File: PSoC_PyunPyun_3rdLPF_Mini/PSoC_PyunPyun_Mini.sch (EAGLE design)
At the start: 28 parts, among them IC1 LM358N

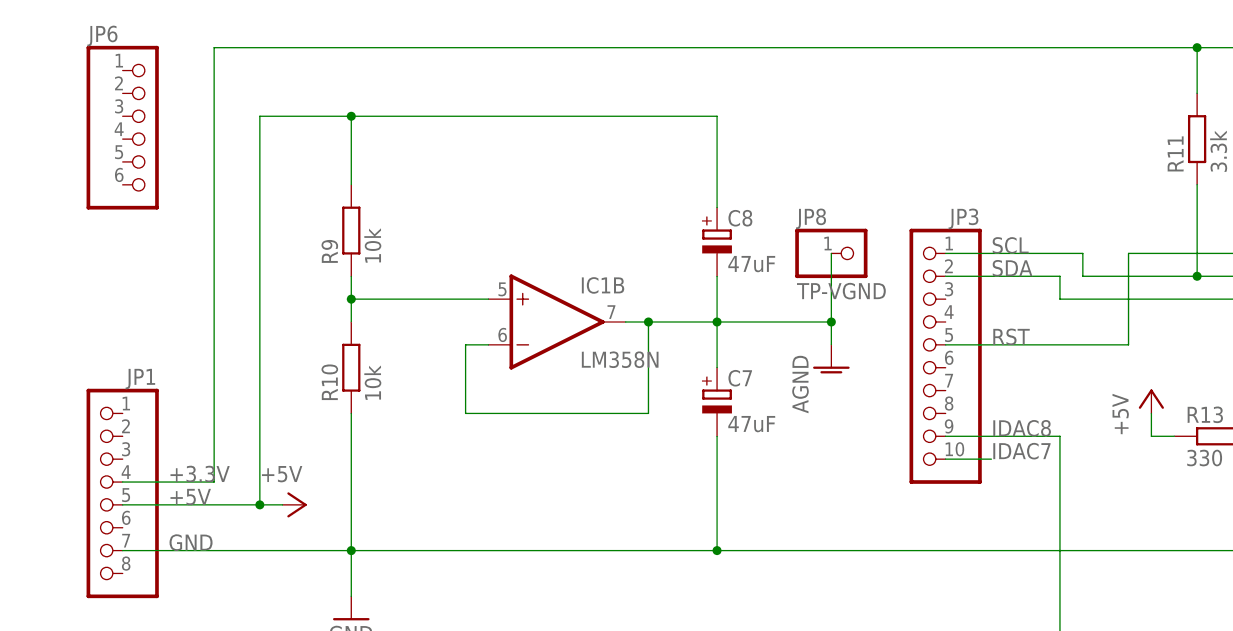
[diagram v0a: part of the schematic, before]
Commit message: PSoC_Pyun_Pyun_Mini 回路図、基板図修正
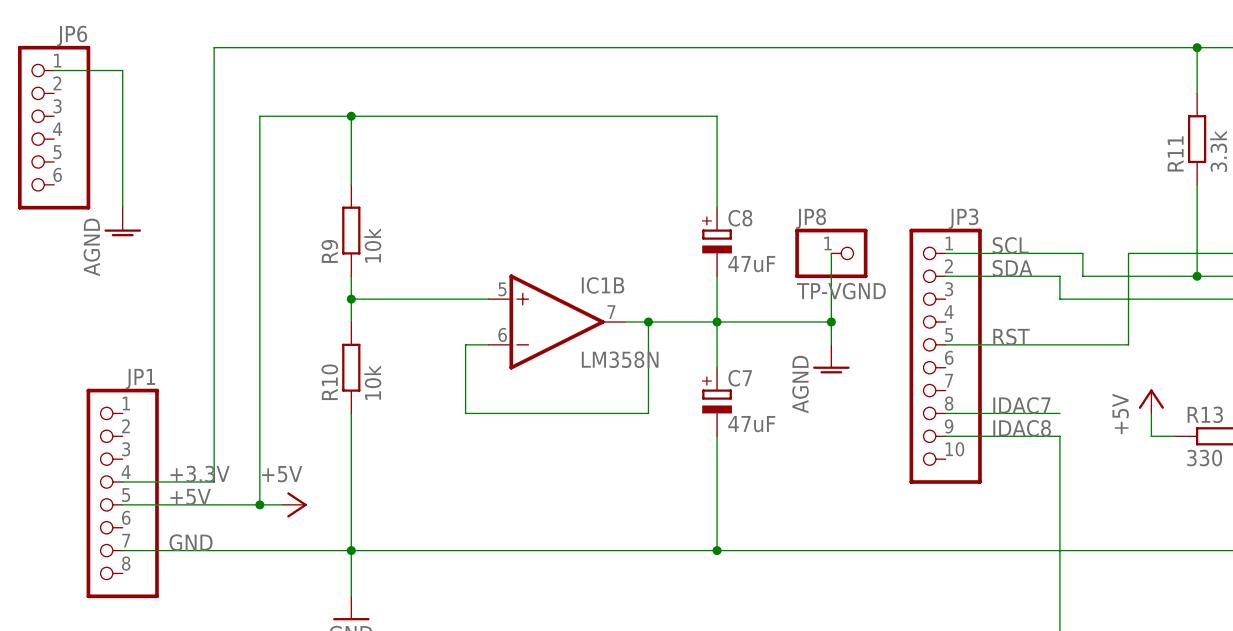
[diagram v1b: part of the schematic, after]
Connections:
- net AGND: now also JP6.1
- net IDAC7: now also JP3.8; no longer JP3.10
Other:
- moved on the sheet: JP6
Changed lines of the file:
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@@
 <part name="JP8" library="pinhead" deviceset="PINHD-1X1" device="" value="TP-VGND"/>
 <part name="JP9" library="pinhead" deviceset="PINHD-1X1" device="" value="TP-GND"/>
+<part name="AGND3" library="supply1" deviceset="AGND" device=""/>
 </parts>
 <sheets>
@@
 <instance part="P+3" gate="1" x="157.48" y="76.2"/>
 <instance part="GND2" gate="VR1" x="170.18" y="45.72"/>
-<instance part="JP6" gate="A" x="12.7" y="144.78"/>
+<instance part="JP6" gate="A" x="0" y="144.78" rot="MR0"/>
 <instance part="IC1" gate="A" x="93.98" y="66.04"/>
 <instance part="IC1" gate="B" x="58.42" y="124.46"/>
@@
 <instance part="JP8" gate="G$1" x="91.44" y="132.08"/>
 <instance part="JP9" gate="G$1" x="154.94" y="96.52"/>
+<instance part="AGND3" gate="VR1" x="10.16" y="134.62"/>
 </instances>
 <busses>
@@
 <wire x1="170.18" y1="55.88" x2="170.18" y2="48.26" width="0.1524" layer="91"/>
 </segment>
+<segment>
+<pinref part="JP6" gate="A" pin="1"/>
+<pinref part="AGND3" gate="VR1" pin="AGND"/>
+<wire x1="2.54" y1="152.4" x2="10.16" y2="152.4" width="0.1524" layer="91"/>
+<wire x1="10.16" y1="152.4" x2="10.16" y2="137.16" width="0.1524" layer="91"/>
+</segment>
 </net>
 <net name="+3.3V" class="0">
@@
 <net name="IDAC7" class="0">
 <segment>
-<pinref part="JP3" gate="A" pin="10"/>
-<wire x1="101.6" y1="109.22" x2="106.68" y2="109.22" width="0.1524" layer="91"/>
-<label x="106.68" y="109.22" size="1.778" layer="95"/>
-</segment>
-</net>
+<pinref part="JP3" gate="A" pin="8"/>
+<wire x1="101.6" y1="114.3" x2="114.3" y2="114.3" width="0.1524" layer="91"/>
+<label x="106.68" y="114.3" size="1.778" layer="95"/>
+</segment>
+</net>

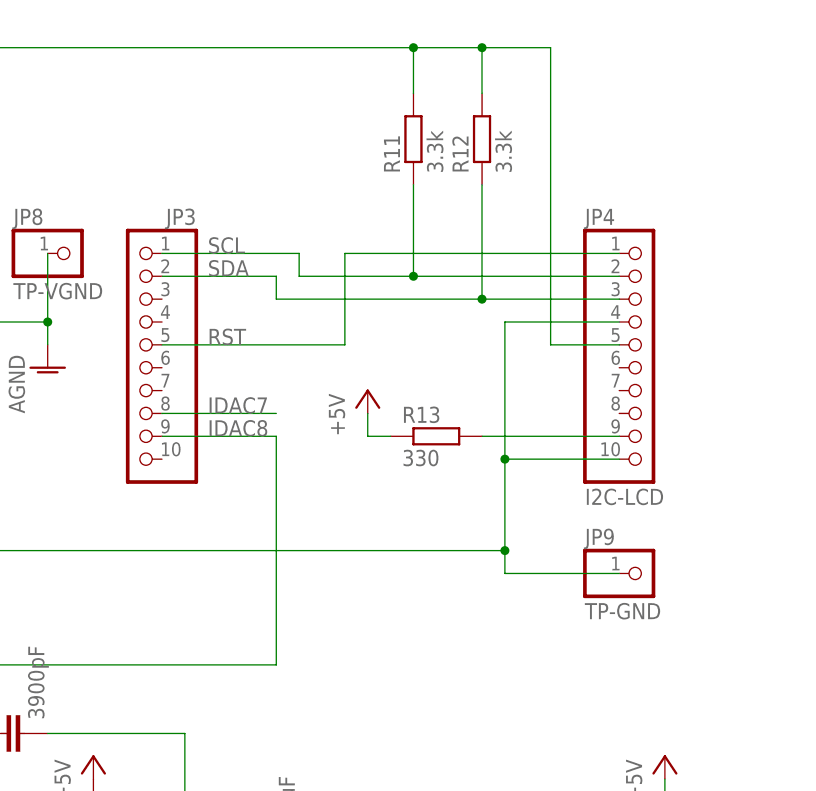
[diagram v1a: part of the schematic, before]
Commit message: PSoC_Pyun_Pyun_3rdLPF_Mini: Change LCD to aitendo
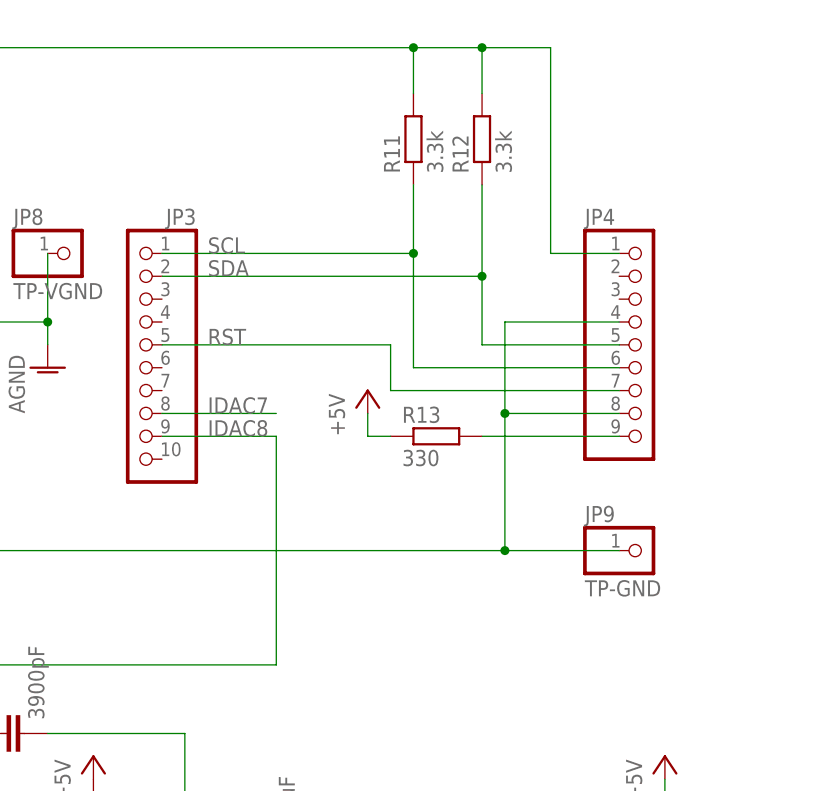
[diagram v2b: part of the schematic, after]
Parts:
- JP4: value I2C-LCD -> (none); device pinhead:PINHD-1X10 -> pinhead:PINHD-1X9
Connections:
- net +3.3V: now also JP4.1; no longer JP4.5
- net GND: now also JP4.8; no longer JP4.10
- net RST: now also JP4.7; no longer JP4.1
- net SCL: now also JP4.6; no longer JP4.2
- net SDA: now also JP4.5; no longer JP4.3
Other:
- moved on the sheet: JP9
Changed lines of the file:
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@@
 <part name="JP2" library="pinhead" deviceset="PINHD-1X8" device=""/>
 <part name="JP3" library="pinhead" deviceset="PINHD-1X10" device=""/>
-<part name="JP4" library="pinhead" deviceset="PINHD-1X10" device="" value="I2C-LCD"/>
 <part name="R1" library="rcl" deviceset="R-EU_" device="0207/7" value="100k"/>
 <part name="R2" library="rcl" deviceset="R-EU_" device="0207/7" value="33k"/>
@@
 <part name="JP9" library="pinhead" deviceset="PINHD-1X1" device="" value="TP-GND"/>
 <part name="AGND3" library="supply1" deviceset="AGND" device=""/>
+<part name="JP4" library="pinhead" deviceset="PINHD-1X9" device=""/>
 </parts>
 <sheets>
@@
 <instance part="JP2" gate="A" x="7.62" y="58.42" rot="MR0"/>
 <instance part="JP3" gate="A" x="99.06" y="121.92" rot="MR0"/>
-<instance part="JP4" gate="A" x="154.94" y="121.92"/>
 <instance part="R1" gate="G$1" x="55.88" y="68.58"/>
 <instance part="R2" gate="G$1" x="71.12" y="68.58"/>
@@
 <instance part="C4" gate="G$1" x="48.26" y="60.96"/>
 <instance part="JP8" gate="G$1" x="91.44" y="132.08"/>
-<instance part="JP9" gate="G$1" x="154.94" y="96.52"/>
+<instance part="JP9" gate="G$1" x="154.94" y="99.06"/>
 <instance part="AGND3" gate="VR1" x="10.16" y="134.62"/>
+<instance part="JP4" gate="A" x="154.94" y="121.92"/>
 </instances>
 <busses>
@@
 <wire x1="76.2" y1="99.06" x2="139.7" y2="99.06" width="0.1524" layer="91"/>
 <junction x="76.2" y="99.06"/>
-<wire x1="139.7" y1="99.06" x2="139.7" y2="109.22" width="0.1524" layer="91"/>
-<pinref part="JP4" gate="A" pin="4"/>
-<wire x1="139.7" y1="109.22" x2="139.7" y2="124.46" width="0.1524" layer="91"/>
+<wire x1="139.7" y1="99.06" x2="139.7" y2="114.3" width="0.1524" layer="91"/>
+<wire x1="139.7" y1="114.3" x2="139.7" y2="124.46" width="0.1524" layer="91"/>
 <wire x1="139.7" y1="124.46" x2="152.4" y2="124.46" width="0.1524" layer="91"/>
 <pinref part="GND1" gate="1" pin="GND"/>
 <wire x1="35.56" y1="93.98" x2="35.56" y2="99.06" width="0.1524" layer="91"/>
-<pinref part="JP4" gate="A" pin="10"/>
-<wire x1="152.4" y1="109.22" x2="139.7" y2="109.22" width="0.1524" layer="91"/>
-<junction x="139.7" y="109.22"/>
 <pinref part="JP9" gate="G$1" pin="1"/>
-<wire x1="152.4" y1="96.52" x2="139.7" y2="96.52" width="0.1524" layer="91"/>
-<wire x1="139.7" y1="96.52" x2="139.7" y2="99.06" width="0.1524" layer="91"/>
+<wire x1="152.4" y1="99.06" x2="139.7" y2="99.06" width="0.1524" layer="91"/>
 <junction x="139.7" y="99.06"/>
+<pinref part="JP4" gate="A" pin="4"/>
+<pinref part="JP4" gate="A" pin="8"/>
+<wire x1="152.4" y1="114.3" x2="139.7" y2="114.3" width="0.1524" layer="91"/>
+<junction x="139.7" y="114.3"/>
 </segment>
 <segment>
@@
 <wire x1="129.54" y1="154.94" x2="137.16" y2="154.94" width="0.1524" layer="91"/>
 <wire x1="137.16" y1="154.94" x2="144.78" y2="154.94" width="0.1524" layer="91"/>
-<wire x1="144.78" y1="154.94" x2="144.78" y2="121.92" width="0.1524" layer="91"/>
-<pinref part="JP4" gate="A" pin="5"/>
-<wire x1="144.78" y1="121.92" x2="152.4" y2="121.92" width="0.1524" layer="91"/>
 <pinref part="R11" gate="G$1" pin="2"/>
 <wire x1="129.54" y1="149.86" x2="129.54" y2="154.94" width="0.1524" layer="91"/>
@@
 <junction x="137.16" y="154.94"/>
 <label x="15.24" y="106.68" size="1.778" layer="95"/>
+<wire x1="144.78" y1="154.94" x2="144.78" y2="132.08" width="0.1524" layer="91"/>
+<pinref part="JP4" gate="A" pin="1"/>
+<wire x1="144.78" y1="132.08" x2="152.4" y2="132.08" width="0.1524" layer="91"/>
 </segment>
 </net>
 <net name="RST" class="0">
 <segment>
-<wire x1="121.92" y1="121.92" x2="121.92" y2="132.08" width="0.1524" layer="91"/>
-<pinref part="JP4" gate="A" pin="1"/>
-<wire x1="121.92" y1="132.08" x2="152.4" y2="132.08" width="0.1524" layer="91"/>
 <pinref part="JP3" gate="A" pin="5"/>
-<wire x1="101.6" y1="121.92" x2="121.92" y2="121.92" width="0.1524" layer="91"/>
+<wire x1="101.6" y1="121.92" x2="127" y2="121.92" width="0.1524" layer="91"/>
 <label x="106.68" y="121.92" size="1.778" layer="95"/>
+<wire x1="127" y1="121.92" x2="127" y2="116.84" width="0.1524" layer="91"/>
+<pinref part="JP4" gate="A" pin="7"/>
+<wire x1="127" y1="116.84" x2="152.4" y2="116.84" width="0.1524" layer="91"/>
 </segment>
 </net>
@@
 <segment>
 <pinref part="JP3" gate="A" pin="1"/>
-<wire x1="101.6" y1="132.08" x2="116.84" y2="132.08" width="0.1524" layer="91"/>
-<wire x1="116.84" y1="132.08" x2="116.84" y2="129.54" width="0.1524" layer="91"/>
-<pinref part="JP4" gate="A" pin="2"/>
-<wire x1="116.84" y1="129.54" x2="129.54" y2="129.54" width="0.1524" layer="91"/>
+<wire x1="101.6" y1="132.08" x2="129.54" y2="132.08" width="0.1524" layer="91"/>
 <pinref part="R11" gate="G$1" pin="1"/>
-<wire x1="129.54" y1="129.54" x2="152.4" y2="129.54" width="0.1524" layer="91"/>
-<wire x1="129.54" y1="139.7" x2="129.54" y2="129.54" width="0.1524" layer="91"/>
-<junction x="129.54" y="129.54"/>
+<wire x1="129.54" y1="139.7" x2="129.54" y2="132.08" width="0.1524" layer="91"/>
 <label x="106.68" y="132.08" size="1.778" layer="95"/>
+<pinref part="JP4" gate="A" pin="6"/>
+<wire x1="152.4" y1="119.38" x2="129.54" y2="119.38" width="0.1524" layer="91"/>
+<wire x1="129.54" y1="119.38" x2="129.54" y2="132.08" width="0.1524" layer="91"/>
+<junction x="129.54" y="132.08"/>
 </segment>
 </net>
@@
 <segment>
 <pinref part="JP3" gate="A" pin="2"/>
-<wire x1="101.6" y1="129.54" x2="114.3" y2="129.54" width="0.1524" layer="91"/>
-<wire x1="114.3" y1="129.54" x2="114.3" y2="127" width="0.1524" layer="91"/>
-<pinref part="JP4" gate="A" pin="3"/>
-<wire x1="114.3" y1="127" x2="137.16" y2="127" width="0.1524" layer="91"/>
+<wire x1="101.6" y1="129.54" x2="137.16" y2="129.54" width="0.1524" layer="91"/>
 <pinref part="R12" gate="G$1" pin="1"/>
-<wire x1="137.16" y1="127" x2="152.4" y2="127" width="0.1524" layer="91"/>
-<wire x1="137.16" y1="139.7" x2="137.16" y2="127" width="0.1524" layer="91"/>
-<junction x="137.16" y="127"/>
+<wire x1="137.16" y1="139.7" x2="137.16" y2="129.54" width="0.1524" layer="91"/>
 <label x="106.68" y="129.54" size="1.778" layer="95"/>
+<pinref part="JP4" gate="A" pin="5"/>
+<wire x1="152.4" y1="121.92" x2="137.16" y2="121.92" width="0.1524" layer="91"/>
+<wire x1="137.16" y1="121.92" x2="137.16" y2="129.54" width="0.1524" layer="91"/>
+<junction x="137.16" y="129.54"/>
 </segment>
 </net>
@@
 <segment>
 <pinref part="R13" gate="G$1" pin="2"/>
+<wire x1="137.16" y1="111.76" x2="152.4" y2="111.76" width="0.1524" layer="91"/>
 <pinref part="JP4" gate="A" pin="9"/>
-<wire x1="137.16" y1="111.76" x2="152.4" y2="111.76" width="0.1524" layer="91"/>
-</segment>
-</net>
+</segment>
+</net>
